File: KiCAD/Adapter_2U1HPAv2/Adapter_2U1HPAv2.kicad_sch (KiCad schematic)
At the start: 2 parts

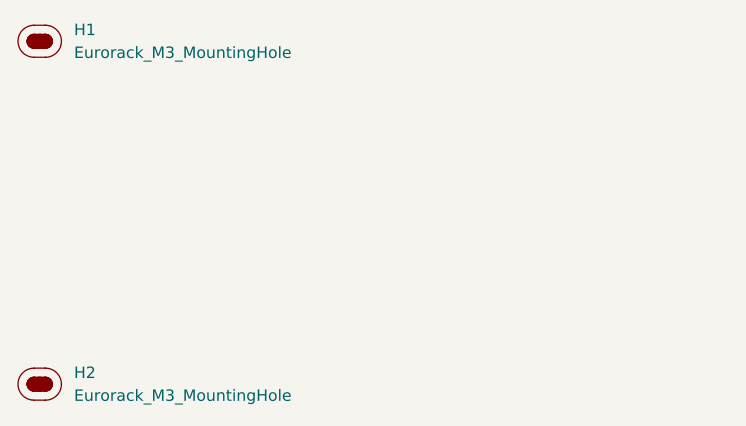
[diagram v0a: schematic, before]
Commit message: added mechanical solder pads to the adapter boards that were missing them. woops!
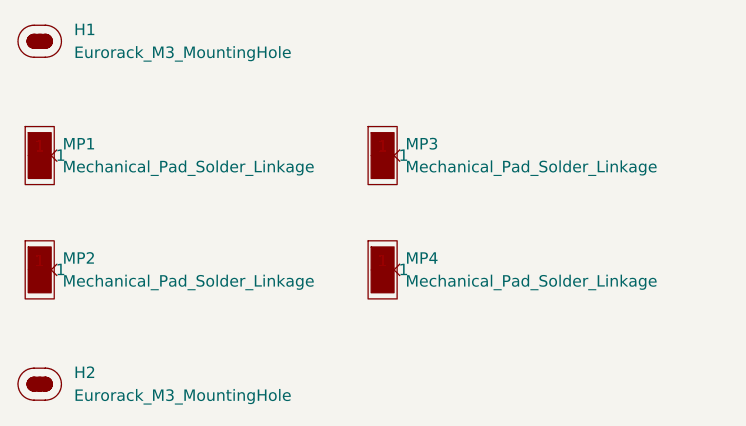
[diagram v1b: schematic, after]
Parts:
- added MP1, MP2, MP3, MP4: Mechanical_Pad_Solder_Linkage, EXC:SolderWirePad_1x01_SMD_1x2mm, symbol EXC:Mechanical_Pad_Solder_Linkage
